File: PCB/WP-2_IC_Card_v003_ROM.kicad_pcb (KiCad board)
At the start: 2 copper layers, 14.5 x 48.5 mm, 6 parts, among them J1 Conn_01x38_Female, U1 FLASH 256Kx8 5v Parallel, U2 FLASH 256Kx8 5v Parallel

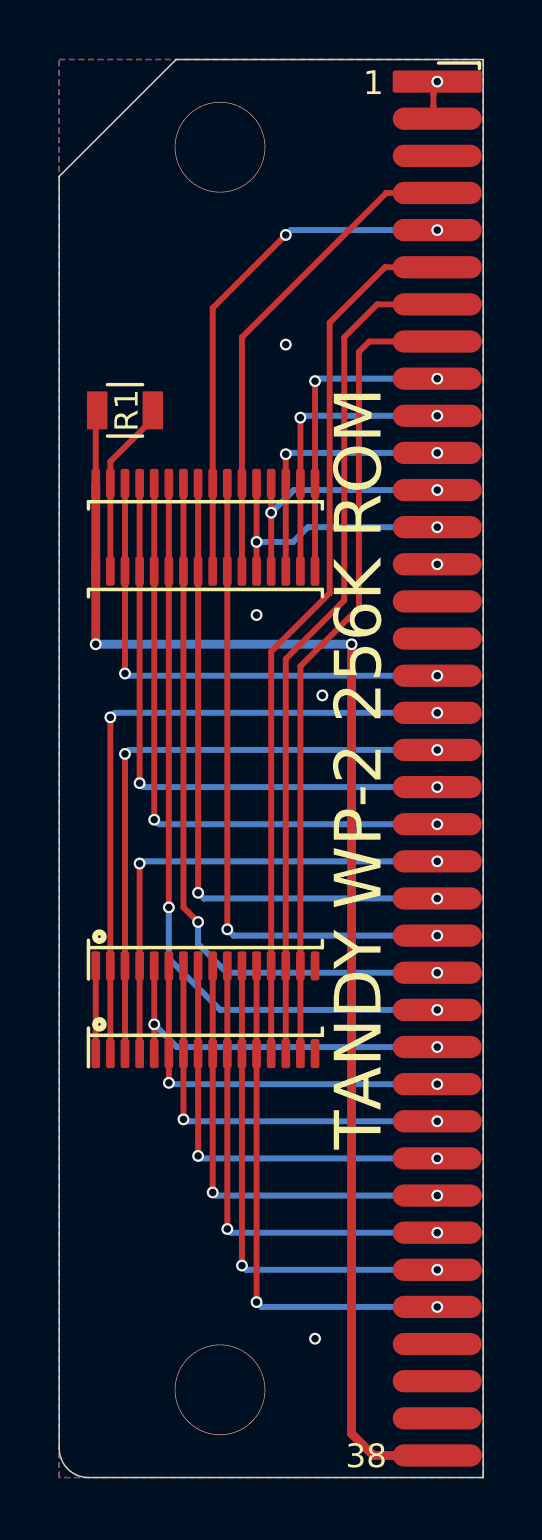
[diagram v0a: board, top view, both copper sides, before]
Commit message: v003_RAM, v003_ROM, ROM programming adapter, v004_RAM_B
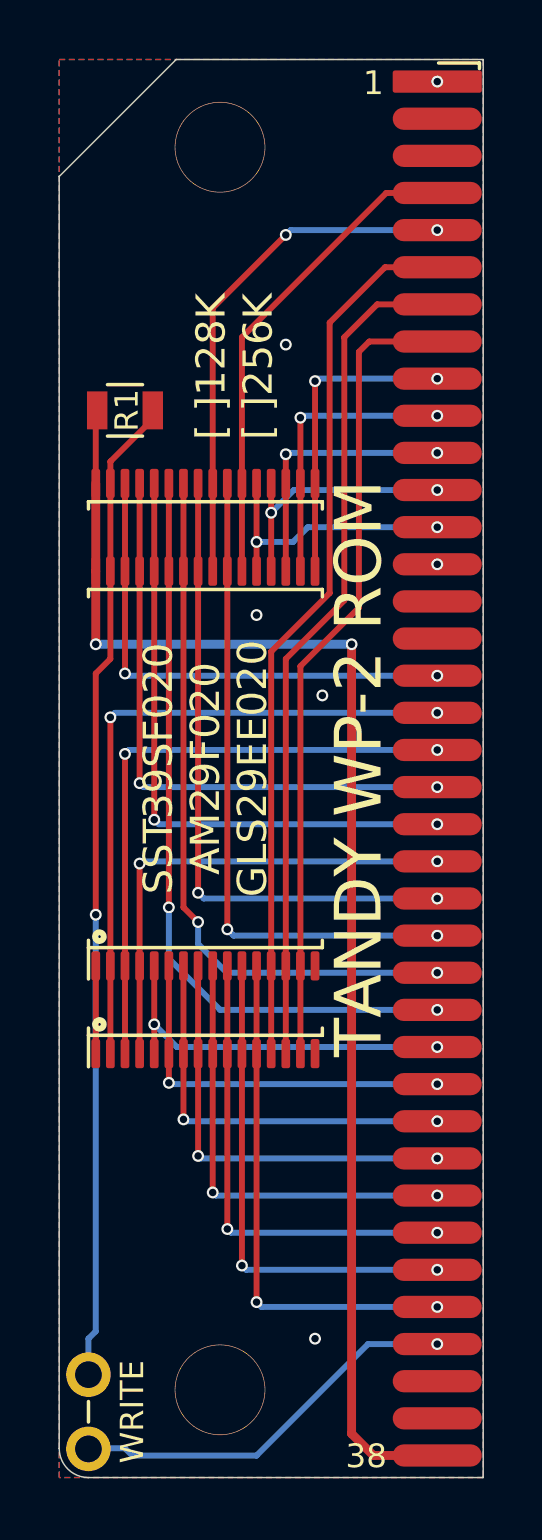
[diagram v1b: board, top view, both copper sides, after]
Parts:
- removed NT1: Net-Tie_2, 0_LOCAL:Net_Tie_2p_8mil
- added JP1: WR_EN, 0_LOCAL:JP2, F.Cu at (145.2, 121.7)
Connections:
- J1 pad 2: /~DET -> (no net)
- J1 pad 35: (no net) -> /R~W
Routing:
- net /~WE: track 6.10 -> 33.9 mm, vias 0 -> 1
- net /R~W: track 0.00 -> 13.6 mm, vias 0 -> 1
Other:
- board text added: "SST39SF020 AM29F020 GLS29EE020"
- board text added: "TANDY WP-2 ROM"
- board text added: "WRITE"
- board text added: "[ ]128K [ ]256K"
- board text removed: "TANDY WP-2 256K ROM"
